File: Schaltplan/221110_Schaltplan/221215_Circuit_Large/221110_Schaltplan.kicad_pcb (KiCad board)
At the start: 2 copper layers, 79.4 x 58.4 mm, 31 parts, among them J0 LDR0, J1 LDR1, J10 LDR2, J11 LDR3, J12 V_solar, J13 V_solar, J14 Dspl GND, J15 Dspl Vcc, J16 Mode Button GND, J17 Poti GND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

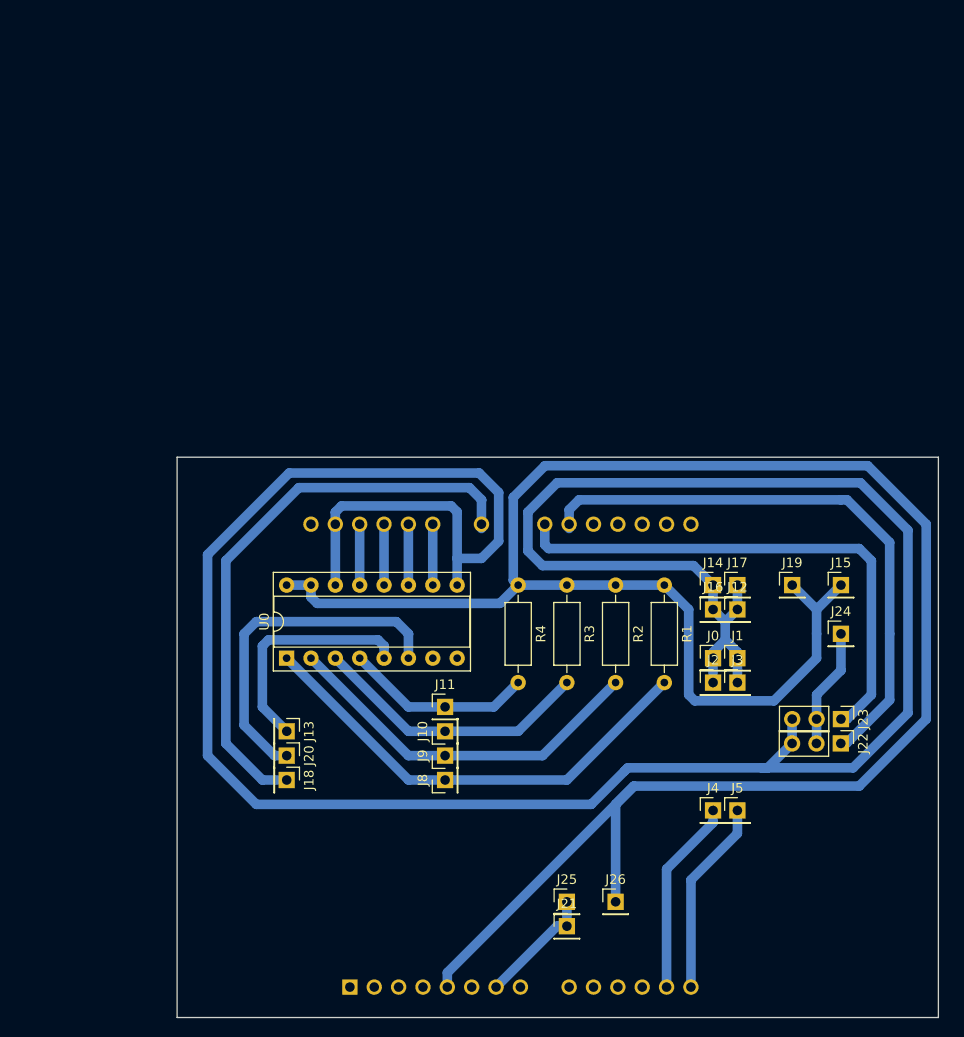
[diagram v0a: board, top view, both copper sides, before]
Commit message: Change CircuitDiagram to match new CAD Design
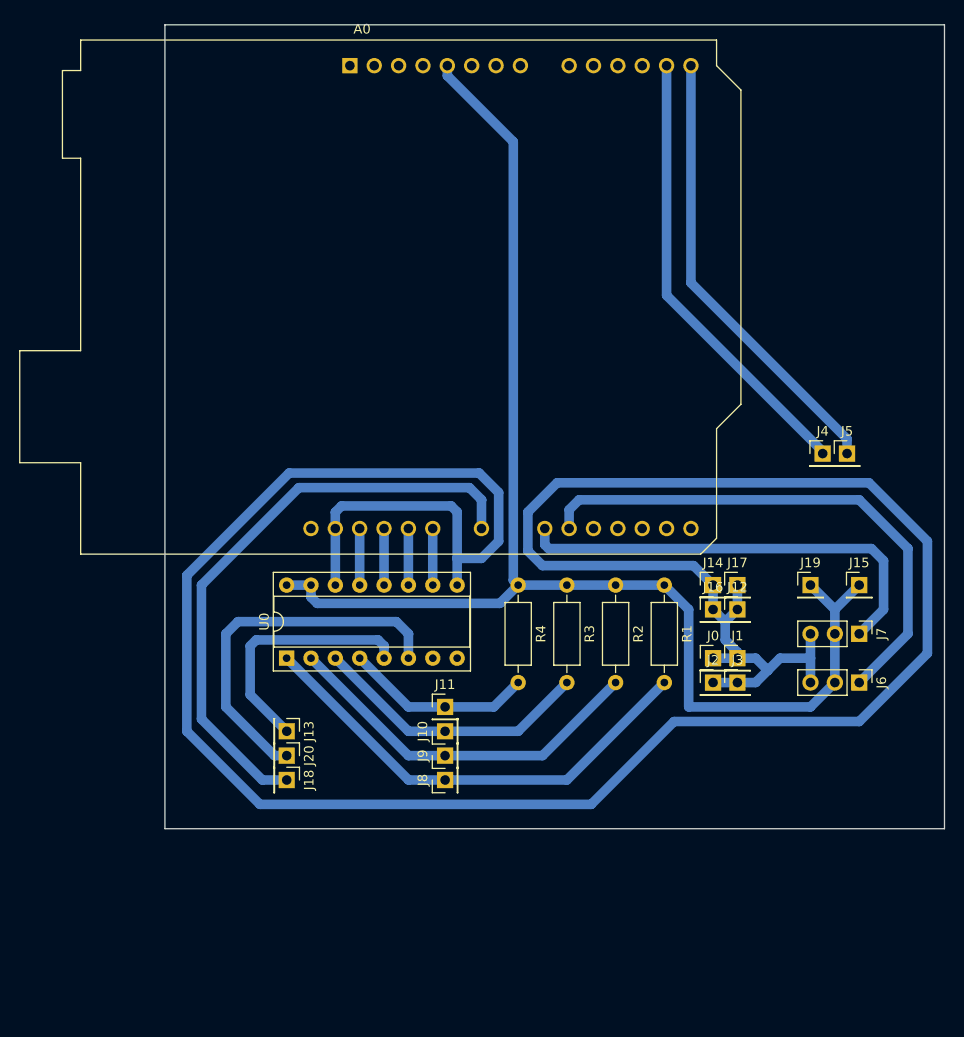
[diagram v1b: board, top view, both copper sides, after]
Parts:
- removed J21, J25: GND, Connector_PinHeader_2.54mm:PinHeader_1x01_P2.54mm_Vertical
- removed J22: Srv0, Connector_PinHeader_2.54mm:PinHeader_1x03_P2.54mm_Vertical
- removed J23: Srv1, Connector_PinHeader_2.54mm:PinHeader_1x03_P2.54mm_Vertical
- removed J24: Vextra, Connector_PinHeader_2.54mm:PinHeader_1x01_P2.54mm_Vertical
- removed J26: 5V, Connector_PinHeader_2.54mm:PinHeader_1x01_P2.54mm_Vertical
- added J6: Srv0, Connector_PinHeader_2.54mm:PinHeader_1x03_P2.54mm_Vertical, F.Cu at (177.8, 124.5)
- added J7: Srv1, Connector_PinHeader_2.54mm:PinHeader_1x03_P2.54mm_Vertical, F.Cu at (177.8, 119.4)
- A0: moved to F.Cu
- moved A0 96.1 mm to (124.7, 60.1)
- moved J4 38.9 mm to (174.0, 100.6)
- moved J5 38.9 mm to (176.5, 100.6)
- moved J15 1.91 mm to (177.8, 114.3)
- moved J19 1.91 mm to (172.7, 114.3)
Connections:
- A0 pad 7: Net-(J21-Pad1) -> unconnected-(A0-Pad7)
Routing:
- net Net-(A0-Pad5): track 233.7 -> 143.8 mm
- net Net-(A0-Pad14): track 20.4 -> 47.2 mm
- net Net-(A0-Pad13): track 20.4 -> 47.2 mm
- net Net-(J21-Pad1): track 12.6 -> 0.00 mm
- net Net-(J24-Pad1): track 12.5 -> 0.00 mm
- net Net-(A0-Pad29): track 287.5 -> 297.1 mm
- net Net-(A0-Pad21): track 54.6 -> 46.4 mm
- net Net-(A0-Pad20): track 61.0 -> 55.9 mm
- net Net-(J20-Pad1): track 36.0 -> 38.7 mm
- net Net-(A0-Pad23): track 60.3 -> 62.4 mm
- net Net-(J13-Pad1): track 24.4 -> 26.2 mm
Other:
- board size 79.4 x 58.4 mm -> 81.3 x 83.8 mm
